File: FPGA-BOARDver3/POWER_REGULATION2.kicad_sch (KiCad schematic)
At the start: 8 parts, among them Q8 FDV301N, U17 NC7WZ07P6X

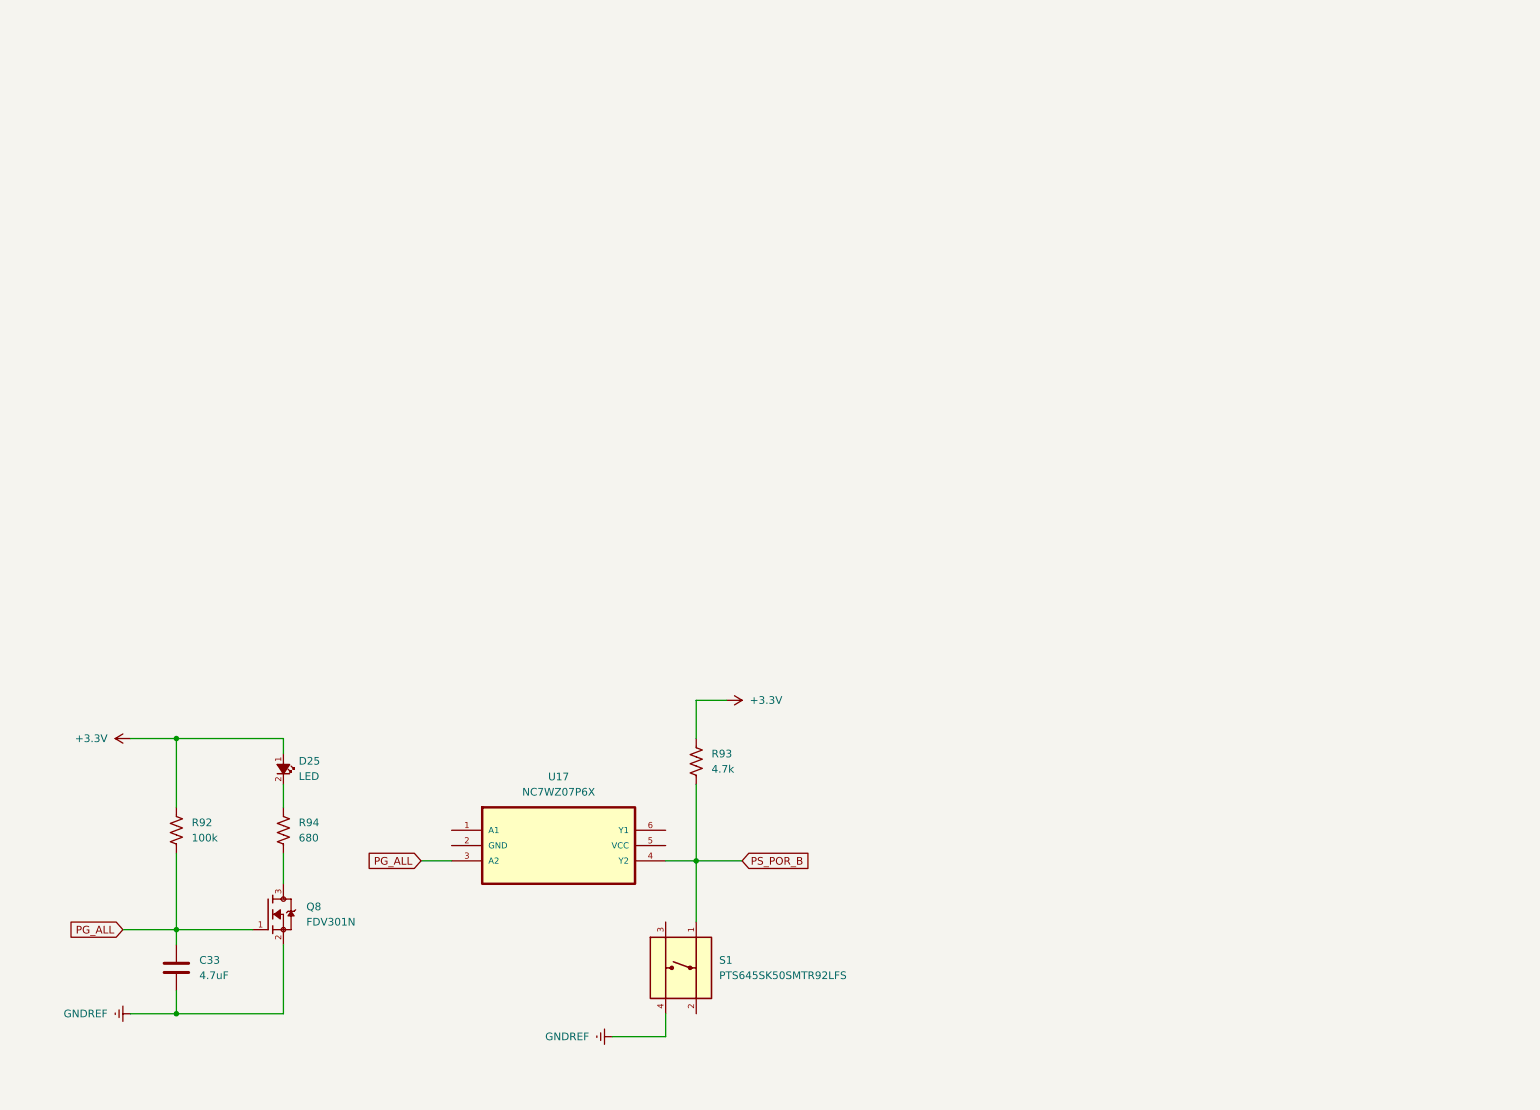
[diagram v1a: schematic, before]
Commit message: Power Regulation sheet 2 added
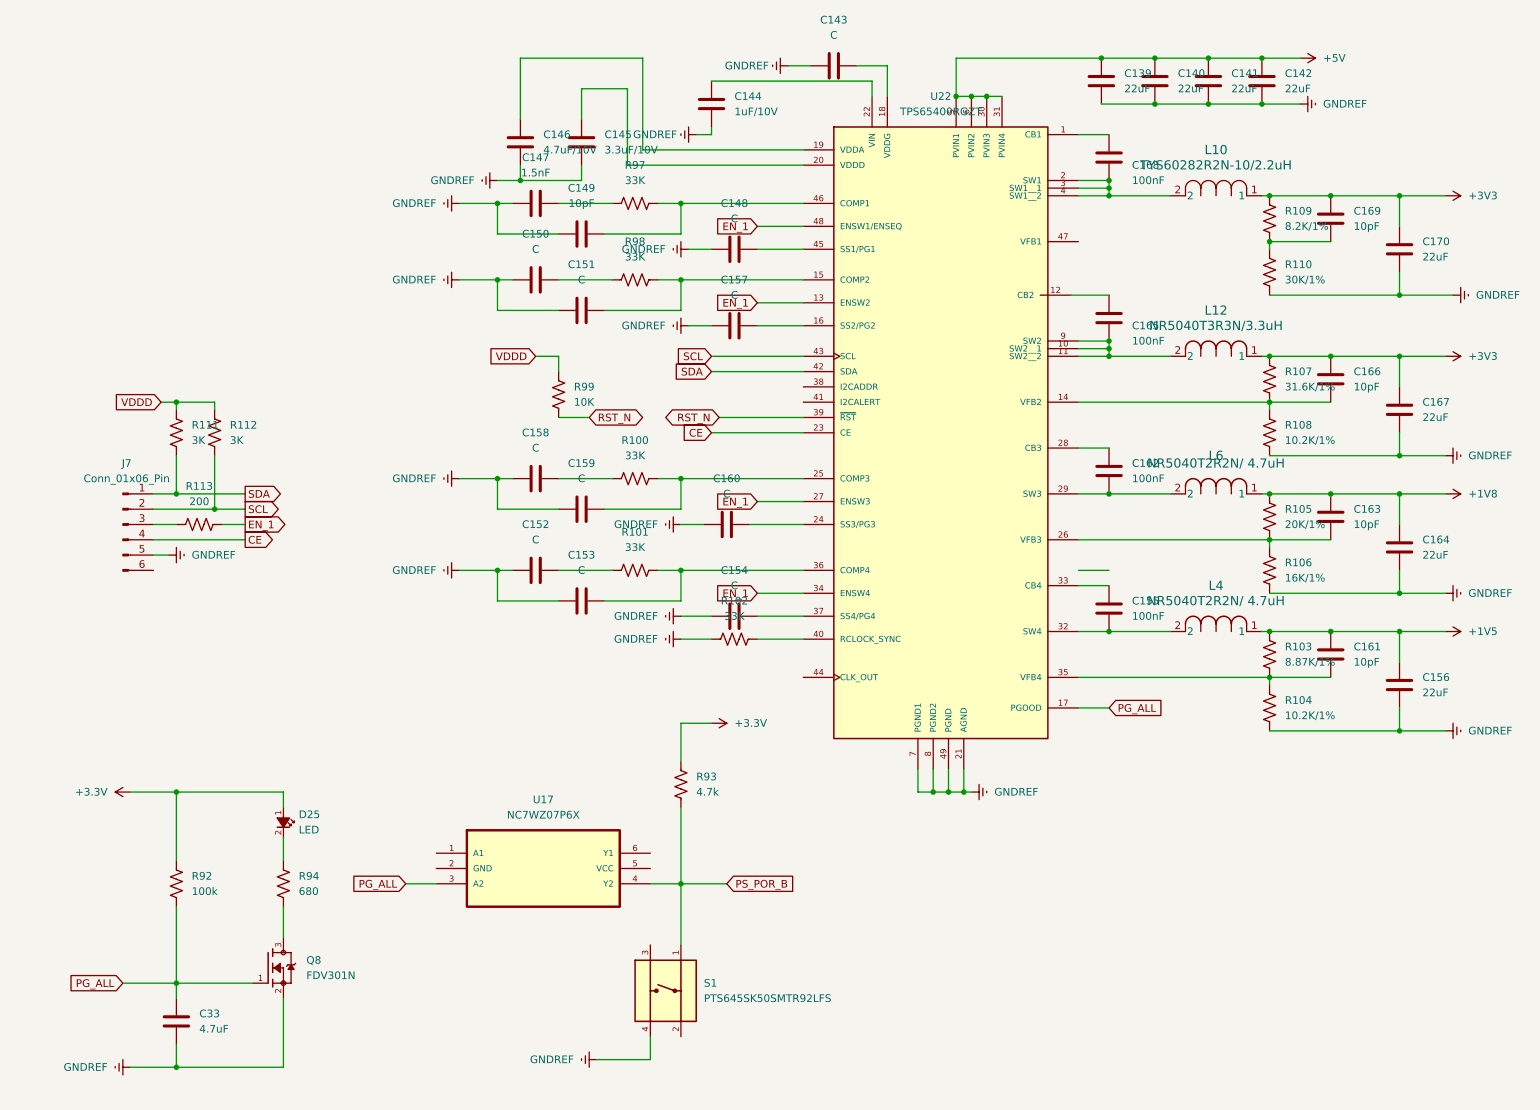
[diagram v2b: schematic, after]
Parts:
- added C139, C140, C141, C142, C156, C164, C167, C170: 22uF, symbol Device:C
- added C143, C148, C150, C151, C152, C153, C154, C157, C158, C159, C160: C, symbol Device:C
- added C144: 1uF/10V, symbol Device:C
- added C145: 3.3uF/10V, symbol Device:C
- added C146: 4.7uF/10V, symbol Device:C
- added C147: 1.5nF, symbol Device:C
- added C149, C161, C163, C166, C169: 10pF, symbol Device:C
- added C155, C162, C165, C168: 100nF, symbol Device:C
- added J7: Conn_01x06_Pin, symbol Connector:Conn_01x06_Pin
- added L10: TYS60282R2N-10/2.2uH, IND_TYS60282_LRD, symbol 2025-03-18_07-11-26:TYS60282R2N-10
- added L12: NR5040T3R3N/3.3uH, IND_TAIYO_NR5040_TAY, symbol 2025-03-18_07-07-44:NR5040T3R3N
- added L4, L6: NR5040T2R2N/ 4.7uH, IND_TAIYO_NR5040_TAY, symbol 2025-03-04_21-33-04:NR5040T2R2N
- added R100, R101, R102, R97, R98: 33K, symbol Device:R_US
- added R103: 8.87K/1%, symbol Device:R_US
- added R104, R108: 10.2K/1%, symbol Device:R_US
- added R105: 20K/1%, symbol Device:R_US
- added R106: 16K/1%, symbol Device:R_US
- added R107: 31.6K/1%, symbol Device:R_US
- added R109: 8.2K/1%, symbol Device:R_US
- added R110: 30K/1%, symbol Device:R_US
- added R111, R112: 3K, symbol Device:R_US
- added R113: 200, symbol Device:R_US
- added R99: 10K, symbol Device:R_US
- added U22: TPS65400RGZT, TPS65400RGZT:QFN50P700X700X100-49N, symbol TPS65400RGZT:TPS65400RGZT
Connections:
- net GNDREF: now also C139.2, C140.2, C141.2, C142.2, C143.1, C144.2, C145.2, C146.2, C147.1, C148.1, C149.1, C150.1, C151.1, C152.1, C153.1, C154.1, C156.2, C157.1, C158.1, C159.1, C160.1, C164.2, C167.2, C170.2, J7.5 (Pin_5), R102.1, R104.2, R106.2, R108.2, R110.2, U22.21 (AGND), U22.49 (PGND), U22.7 (PGND1), U22.8 (PGND2)
- net PG_ALL: now also U22.17 (PGOOD)
- new net: C143.2, U22.18 (VDDG)
- new net: C147.2, R97.1
- new net: C149.2, R97.2, U22.46 (COMP1)
- new net: C163.2, R105.2, R106.1, U22.26 (VFB3)
- new net: C168.1, U22.1 (CB1)
- new net: C165.2, L12.2, U22.10 (SW2__1), U22.11 (SW2__2), U22.9 (SW2)
- new net: C165.1, U22.12 (CB2)
- new net: C166.2, R107.2, R108.1, U22.14 (VFB2)
- new net: C151.2, R98.2, U22.15 (COMP2)
- new net: C157.2, U22.16 (SS2/PG2)
- new net: C146.1, U22.19 (VDDA)
- new net: C168.2, L10.2, U22.2 (SW1), U22.3 (SW1__1), U22.4 (SW1__2)
- new net: C145.1, U22.20 (VDDD)
- new net: C144.1, U22.22 (VIN)
- new net: C160.2, U22.24 (SS3/PG3)
- new net: C159.2, R100.2, U22.25 (COMP3)
- new net: C162.1, U22.28 (CB3)
- new net: C162.2, L6.2, U22.29 (SW3)
- new net: C155.2, L4.2, U22.32 (SW4)
- new net: C155.1, U22.33 (CB4)
- new net: C161.2, R103.2, R104.1, U22.35 (VFB4)
- new net: C153.2, R101.2, U22.36 (COMP4)
- new net: C154.2, U22.37 (SS4/PG4)
- new net: R102.2, U22.40 (RCLOCK_SYNC)
- new net: C148.2, U22.45 (SS1/PG1)
- new net: C158.2, R100.1
- new net: C169.2, R109.2, R110.1
- new net: C152.2, R101.1
- new net: J7.3 (Pin_3), R113.1
- new net: C150.2, R98.1
- new net +1V5: C156.1, C161.1, L4.1, R103.1
- new net +1V8: C163.1, C164.1, L6.1, R105.1
- new net +3V3: C166.1, C167.1, C169.1, C170.1, L10.1, L12.1, R107.1, R109.1
- new net +5V: C139.1, C140.1, C141.1, C142.1, U22.30 (PVIN3), U22.31 (PVIN4), U22.5 (PVIN1), U22.6 (PVIN2)
- new net CE: J7.4 (Pin_4), U22.23 (CE)
- new net EN_1: R113.2, U22.13 (ENSW2), U22.27 (ENSW3), U22.34 (ENSW4), U22.48 (ENSW1/ENSEQ)
- new net RST_N: R99.1, U22.39 (~{RST})
- new net SCL: J7.2 (Pin_2), R112.2, U22.43 (SCL)
- new net SDA: J7.1 (Pin_1), R111.2, U22.42 (SDA)
- new net VDDD: R111.1, R112.1, R99.2
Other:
- moved on the sheet: C33, D25, Q8, R92, R93, R94, S1, U17

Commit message: assigned footprints for power section and ddr3
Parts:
- C139, C140, C141, C142, C143, C144, C145, C146, C147, C148, C149, C150, C151, C152, C153, C154, C155, C156, C157, C158, C159, C160, C161, C162, C163, C164, C165, C166, C167, C168, C169, C170, C33: footprint (none) -> JLCPCB:C_0402
- D25: footprint (none) -> LED_SMD:LED_0402_1005Metric
- L10: footprint IND_TYS60282_LRD -> TYS60282R2N_10:IND_TYS60282_LRD
- L12, L4, L6: footprint IND_TAIYO_NR5040_TAY -> footprints:IND_TAIYO_NR5040_TAY
- R100, R101, R102, R103, R104, R105, R106, R107, R108, R109, R110, R111, R112, R113, R92, R93, R94, R97, R98, R99: footprint (none) -> JLCPCB:R_0402
- U22: footprint TPS65400RGZT:QFN50P700X700X100-49N -> tps65400rgzt:RGZ0048B

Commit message: footprints added to project specific library
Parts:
- C139, C140, C141, C142, C143, C144, C145, C146, C147, C148, C149, C150, C151, C152, C153, C154, C155, C156, C157, C158, C159, C160, C161, C162, C163, C164, C165, C166, C167, C168, C169, C170, C33: footprint JLCPCB:C_0402 -> footprints:C_0402
- L10: footprint TYS60282R2N_10:IND_TYS60282_LRD -> footprints:IND_TYS60282_LRD
- Q8: footprint FDV301N:SOT95P237X111-3N -> footprints:FDV301N
- R100, R101, R102, R103, R104, R105, R106, R107, R108, R109, R110, R111, R112, R113, R92, R93, R94, R97, R98, R99: footprint JLCPCB:R_0402 -> footprints:R_0402
- U17: footprint NC7WZ07P6X:SOT65P210X110-6N -> footprints:NC7WZ07P6X
- U22: footprint tps65400rgzt:RGZ0048B -> footprints:RGZ0048B
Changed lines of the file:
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@@
 			)
 		)
-		(property "Footprint" "JLCPCB:C_0402"
+		(property "Footprint" "footprints:C_0402"
 			(at 149.86 15.5448 0)
 			(effects
@@
 			)
 		)
-		(property "Footprint" "JLCPCB:R_0402"
+		(property "Footprint" "footprints:R_0402"
 			(at 113.284 38.354 90)
 			(effects
@@
 			)
 		)
-		(property "Footprint" "JLCPCB:R_0402"
+		(property "Footprint" "footprints:R_0402"
 			(at 99.314 70.866 90)
 			(effects
@@
 			)
 		)
-		(property "Footprint" "JLCPCB:R_0402"
+		(property "Footprint" "footprints:R_0402"
 			(at 219.456 91.694 90)
 			(effects
@@
 			)
 		)
-		(property "Footprint" "JLCPCB:C_0402"
+		(property "Footprint" "footprints:C_0402"
 			(at 240.9952 77.47 0)
 			(effects
@@
 			)
 		)
-		(property "Footprint" "tps65400rgzt:RGZ0048B"
+		(property "Footprint" "footprints:RGZ0048B"
 			(at 164.338 36.83 0)
 			(effects
@@
 			)
 		)
-		(property "Footprint" "JLCPCB:C_0402"
+		(property "Footprint" "footprints:C_0402"
 			(at 100.33 38.4048 0)
 			(effects
@@
 			)
 		)
-		(property "Footprint" "JLCPCB:R_0402"
+		(property "Footprint" "footprints:R_0402"
 			(at 113.284 84.074 90)
 			(effects
@@
 			)
 		)
-		(property "Footprint" "JLCPCB:C_0402"
+		(property "Footprint" "footprints:C_0402"
 			(at 133.35 46.0248 0)
 			(effects
@@
 			)
 		)
-		(property "Footprint" "JLCPCB:C_0402"
+		(property "Footprint" "footprints:C_0402"
 			(at 218.1352 22.86 0)
 			(effects
@@
 			)
 		)
-		(property "Footprint" "JLCPCB:C_0402"
+		(property "Footprint" "footprints:C_0402"
 			(at 133.35 58.7248 0)
 			(effects
@@
 			)
 		)
-		(property "Footprint" "JLCPCB:C_0402"
+		(property "Footprint" "footprints:C_0402"
 			(at 240.9952 50.8 0)
 			(effects
@@
 			)
 		)
-		(property "Footprint" "JLCPCB:R_0402"
+		(property "Footprint" "footprints:R_0402"
 			(at 129.794 110.744 90)
 			(effects
@@
 			)
 		)
-		(property "Footprint" "JLCPCB:C_0402"
+		(property "Footprint" "footprints:C_0402"
 			(at 126.6952 26.67 0)
 			(effects
@@
 			)
 		)
-		(property "Footprint" "JLCPCB:C_0402"
+		(property "Footprint" "footprints:C_0402"
 			(at 191.4652 22.86 0)
 			(effects
@@
 			)
 		)
-		(property "Footprint" "JLCPCB:C_0402"
+		(property "Footprint" "footprints:C_0402"
 			(at 107.95 104.4448 0)
 			(effects
@@
 			)
 		)
-		(property "Footprint" "JLCPCB:R_0402"
+		(property "Footprint" "footprints:R_0402"
 			(at 219.456 123.444 90)
 			(effects
@@
 			)
 		)
-		(property "Footprint" "JLCPCB:R_0402"
+		(property "Footprint" "footprints:R_0402"
 			(at 219.456 42.164 90)
 			(effects
@@
 			)
 		)
-		(property "Footprint" "JLCPCB:C_0402"
+		(property "Footprint" "footprints:C_0402"
 			(at 240.9952 123.19 0)
 			(effects
@@
 			)
 		)
-		(property "Footprint" "JLCPCB:R_0402"
+		(property "Footprint" "footprints:R_0402"
 			(at 37.846 152.654 90)
 			(effects
@@
 			)
 		)
-		(property "Footprint" "JLCPCB:R_0402"
+		(property "Footprint" "footprints:R_0402"
 			(at 113.284 99.314 90)
 			(effects
@@
 			)
 		)
-		(property "Footprint" "JLCPCB:R_0402"
+		(property "Footprint" "footprints:R_0402"
 			(at 37.846 77.724 90)
 			(effects
@@
 			)
 		)
-		(property "Footprint" "JLCPCB:R_0402"
+		(property "Footprint" "footprints:R_0402"
 			(at 219.456 100.584 90)
 			(effects
@@
 			)
 		)
-		(property "Footprint" "JLCPCB:R_0402"
+		(property "Footprint" "footprints:R_0402"
 			(at 55.626 152.654 90)
 			(effects
@@
 			)
 		)
-		(property "Footprint" "JLCPCB:R_0402"
+		(property "Footprint" "footprints:R_0402"
 			(at 44.196 77.724 90)
 			(effects
@@
 			)
 		)
-		(property "Footprint" "JLCPCB:C_0402"
+		(property "Footprint" "footprints:C_0402"
 			(at 100.33 84.1248 0)
 			(effects
@@
 			)
 		)
-		(property "Footprint" "JLCPCB:C_0402"
+		(property "Footprint" "footprints:C_0402"
 			(at 133.35 106.9848 0)
 			(effects
@@
 			)
 		)
-		(property "Footprint" "JLCPCB:R_0402"
+		(property "Footprint" "footprints:R_0402"
 			(at 219.456 114.554 90)
 			(effects
@@
 			)
 		)
-		(property "Footprint" "JLCPCB:C_0402"
+		(property "Footprint" "footprints:C_0402"
 			(at 229.5652 118.11 0)
 			(effects
@@
 			)
 		)
-		(property "Footprint" "JLCPCB:C_0402"
+		(property "Footprint" "footprints:C_0402"
 			(at 105.1052 33.02 0)
 			(effects
@@
 			)
 		)
-		(property "Footprint" "JLCPCB:C_0402"
+		(property "Footprint" "footprints:C_0402"
 			(at 37.7952 179.07 0)
 			(effects
@@
 			)
 		)
-		(property "Footprint" "JLCPCB:C_0402"
+		(property "Footprint" "footprints:C_0402"
 			(at 100.33 99.3648 0)
 			(effects
@@
 			)
 		)
-		(property "Footprint" "JLCPCB:C_0402"
+		(property "Footprint" "footprints:C_0402"
 			(at 132.08 91.7448 0)
 			(effects
@@
 			)
 		)
-		(property "Footprint" "JLCPCB:C_0402"
+		(property "Footprint" "footprints:C_0402"
 			(at 192.7352 110.49 0)
 			(effects
@@
 			)
 		)
-		(property "Footprint" "JLCPCB:C_0402"
+		(property "Footprint" "footprints:C_0402"
 			(at 200.3552 22.86 0)
 			(effects
@@
 			)
 		)
-		(property "Footprint" "NC7WZ07P6X:SOT65P210X110-6N"
+		(property "Footprint" "footprints:NC7WZ07P6X"
 			(at 97.79 151.13 0)
 			(effects
@@
 			)
 		)
-		(property "Footprint" "JLCPCB:C_0402"
+		(property "Footprint" "footprints:C_0402"
 			(at 229.5652 45.72 0)
 			(effects
@@
 			)
 		)
-		(property "Footprint" "JLCPCB:R_0402"
+		(property "Footprint" "footprints:R_0402"
 			(at 121.666 136.144 90)
 			(effects
@@
 			)
 		)
-		(property "Footprint" "JLCPCB:C_0402"
+		(property "Footprint" "footprints:C_0402"
 			(at 209.2452 22.86 0)
 			(effects
@@
 			)
 		)
-		(property "Footprint" "JLCPCB:C_0402"
+		(property "Footprint" "footprints:C_0402"
 			(at 107.95 89.2048 0)
 			(effects
@@
 			)
 		)
-		(property "Footprint" "JLCPCB:R_0402"
+		(property "Footprint" "footprints:R_0402"
 			(at 219.456 68.834 90)
 			(effects
@@
 			)
 		)
-		(property "Footprint" "JLCPCB:C_0402"
+		(property "Footprint" "footprints:C_0402"
 			(at 107.95 43.4848 0)
 			(effects
@@
 			)
 		)
-		(property "Footprint" "JLCPCB:C_0402"
+		(property "Footprint" "footprints:C_0402"
 			(at 192.7352 62.23 0)
 			(effects
@@
 			)
 		)
-		(property "Footprint" "JLCPCB:C_0402"
+		(property "Footprint" "footprints:C_0402"
 			(at 192.7352 87.63 0)
 			(effects
@@
 			)
 		)
-		(property "Footprint" "TYS60282R2N_10:IND_TYS60282_LRD"
+		(property "Footprint" "footprints:IND_TYS60282_LRD"
 			(at 201.93 38.1 0)
 			(effects
@@
 			)
 		)
-		(property "Footprint" "JLCPCB:C_0402"
+		(property "Footprint" "footprints:C_0402"
 			(at 229.5652 72.39 0)
 			(effects
@@
 			)
 		)
-		(property "Footprint" "JLCPCB:C_0402"
+		(property "Footprint" "footprints:C_0402"
 			(at 229.5652 95.25 0)
 			(effects
@@
 			)
 		)
-		(property "Footprint" "JLCPCB:C_0402"
+		(property "Footprint" "footprints:C_0402"
 			(at 94.9452 33.02 0)
 			(effects
@@
 			)
 		)
-		(property "Footprint" "JLCPCB:R_0402"
+		(property "Footprint" "footprints:R_0402"
 			(at 219.456 77.724 90)
 			(effects
@@
 			)
 		)
-		(property "Footprint" "JLCPCB:R_0402"
+		(property "Footprint" "footprints:R_0402"
 			(at 219.456 51.054 90)
 			(effects
@@
 			)
 		)
-		(property "Footprint" "JLCPCB:C_0402"
+		(property "Footprint" "footprints:C_0402"
 			(at 240.9952 100.33 0)
 			(effects
@@
 			)
 		)
-		(property "Footprint" "FDV301N:SOT95P237X111-3N"
+		(property "Footprint" "footprints:FDV301N"
 			(at 52.07 166.37 0)
 			(effects
@@
 			)
 		)
-		(property "Footprint" "JLCPCB:R_0402"
+		(property "Footprint" "footprints:R_0402"
 			(at 113.284 51.054 90)
 			(effects
@@
 			)
 		)
-		(property "Footprint" "JLCPCB:R_0402"
+		(property "Footprint" "footprints:R_0402"
 			(at 40.894 91.694 90)
 			(effects
@@
 			)
 		)
-		(property "Footprint" "JLCPCB:C_0402"
+		(property "Footprint" "footprints:C_0402"
 			(at 100.33 51.1048 0)
 			(effects
@@
 			)
 		)
-		(property "Footprint" "JLCPCB:C_0402"
+		(property "Footprint" "footprints:C_0402"
 			(at 107.95 56.1848 0)
 			(effects
@@
 			)
 		)
-		(property "Footprint" "JLCPCB:C_0402"
+		(property "Footprint" "footprints:C_0402"
 			(at 192.7352 35.56 0)
 			(effects

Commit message: spdif fpga bansks
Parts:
- removed U17: NC7WZ07P6X, footprints:NC7WZ07P6X, symbol NC7WZ07P6X:NC7WZ07P6X
- added U4: NC7WZ07P6X, footprints:NC7WZ07P6X, symbol NC7WZ07P6X:NC7WZ07P6X
- C143: value C -> 10uF/10V
- C148, C154, C157, C160: value C -> 33nF
- C150: value C -> 150pF
- C151, C153, C159: value C -> 10pF
- C152: value C -> 1.2nF
- C158: value C -> 330pF
- J7: footprint (none) -> footprints:CONN6_PZ254V-11-06P_XFC
- S1: footprint PTS645SK50SMTR92LFS:SW_PTS645SK50SMTR92LFS -> footprints:SW_PTS645SK50SMTR92LFS
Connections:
- net GNDREF: now also S1.3; no longer S1.4
- net PG_ALL: now also U4.3 (A2)
- net PS_POR_B: now also U4.4 (Y2)
